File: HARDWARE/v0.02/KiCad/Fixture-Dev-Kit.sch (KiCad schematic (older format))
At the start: 6 parts, among them J1 DUT, J2 POWER, J39 DUT BAT, J40 DUT BAT

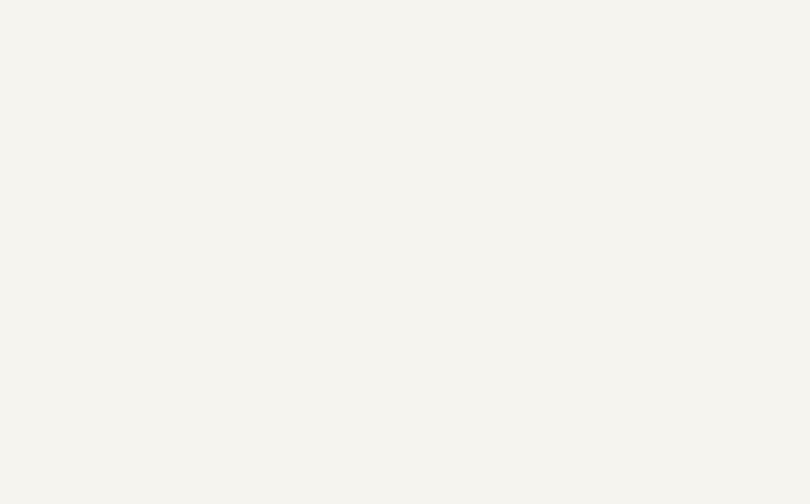
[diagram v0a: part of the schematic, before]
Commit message: adding latest updates from pcb layout designed 11/8/2017
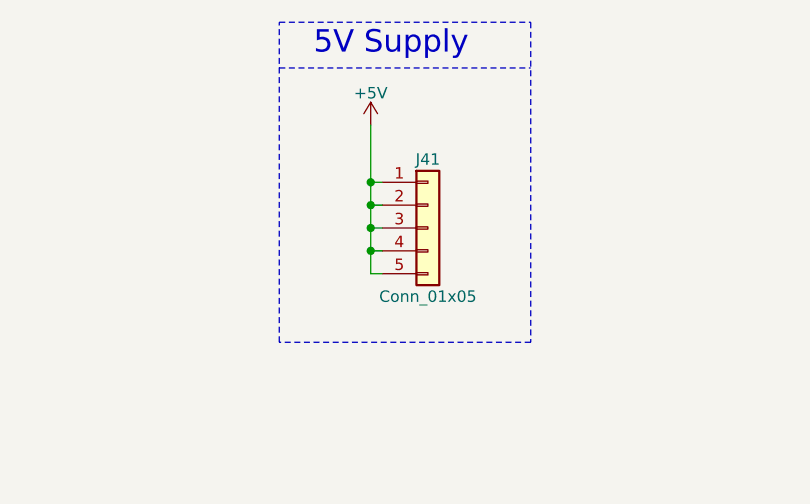
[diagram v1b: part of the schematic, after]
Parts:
- added J41: Conn_01x05, Pin_Headers:Pin_Header_Angled_1x05_Pitch2.54mm, symbol Conn_01x05
- J39: footprint Connectors_JST:JST_PH_B2B-PH-K_02x2.00mm_Straight -> Connectors_JST:JST_PH_S2B-PH-K_02x2.00mm_Angled
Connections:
- wire segments 50 -> 56
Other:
- note added: "5V Supply\n"
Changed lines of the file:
@@
 LIBS:TCA6424ARGJR
 LIBS:USB-A1HSW6
+LIBS:jumper
 LIBS:Fixture-Dev-Kit-cache
 EELAYER 25 0
@@
 $EndComp
 $Comp
-L GND #PWR9
+L GND #PWR2
 U 1 1 59EFDED6
 P 1700 5100
-F 0 "#PWR9" H 1700 4850 50  0001 C CNN
+F 0 "#PWR2" H 1700 4850 50  0001 C CNN
 F 1 "GND" H 1700 4950 50  0000 C CNN
 F 2 "" H 1700 5100 50  0001 C CNN
@@
 	1550 4350 1800 4350
 $Comp
-L GND #PWR7
+L GND #PWR4
 U 1 1 59F1B0B1
 P 1800 4450
-F 0 "#PWR7" H 1800 4200 50  0001 C CNN
+F 0 "#PWR4" H 1800 4200 50  0001 C CNN
 F 1 "GND" H 1800 4300 50  0000 C CNN
 F 2 "" H 1800 4450 50  0001 C CNN
@@
 	850  4000 2550 4000
 $Comp
-L +5V #PWR8
+L +5V #PWR1
 U 1 1 59F1DD6A
 P 1200 5100
-F 0 "#PWR8" H 1200 4950 50  0001 C CNN
+F 0 "#PWR1" H 1200 4950 50  0001 C CNN
 F 1 "+5V" H 1200 5240 50  0000 C CNN
 F 2 "" H 1200 5100 50  0001 C CNN
@@
 $EndComp
 $Comp
-L +5V #PWR6
+L +5V #PWR3
 U 1 1 59F1DD81
 P 1800 4350
-F 0 "#PWR6" H 1800 4200 50  0001 C CNN
+F 0 "#PWR3" H 1800 4200 50  0001 C CNN
 F 1 "+5V" H 1800 4490 50  0000 C CNN
 F 2 "" H 1800 4350 50  0001 C CNN
@@
 $EndSheet
 $Comp
-L GND #PWR5
+L GND #PWR10
 U 1 1 59FA7F5A
 P 9250 4050
-F 0 "#PWR5" H 9250 3800 50  0001 C CNN
+F 0 "#PWR10" H 9250 3800 50  0001 C CNN
 F 1 "GND" H 9250 3900 50  0000 C CNN
 F 2 "" H 9250 4050 50  0001 C CNN
@@
 	2650 1600 2500 1600
 $Comp
-L +5V #PWR1
+L +5V #PWR5
 U 1 1 59FB980B
 P 2650 1950
-F 0 "#PWR1" H 2650 1800 50  0001 C CNN
+F 0 "#PWR5" H 2650 1800 50  0001 C CNN
 F 1 "+5V" H 2650 2090 50  0000 C CNN
 F 2 "" H 2650 1950 50  0001 C CNN
@@
 	6850 3200 6700 3200
 $Comp
-L +5V #PWR3
+L +5V #PWR6
 U 1 1 59FC47B7
 P 4500 3050
-F 0 "#PWR3" H 4500 2900 50  0001 C CNN
+F 0 "#PWR6" H 4500 2900 50  0001 C CNN
 F 1 "+5V" H 4500 3190 50  0000 C CNN
 F 2 "" H 4500 3050 50  0001 C CNN
@@
 $EndComp
 $Comp
-L +5V #PWR4
+L +5V #PWR8
 U 1 1 59FC49D9
 P 6900 3100
-F 0 "#PWR4" H 6900 2950 50  0001 C CNN
+F 0 "#PWR8" H 6900 2950 50  0001 C CNN
 F 1 "+5V" H 6900 3240 50  0000 C CNN
 F 2 "" H 6900 3100 50  0001 C CNN
@@
 F 0 "J39" H 8400 4550 50  0000 C CNN
 F 1 "DUT BAT" H 8400 4250 50  0000 C CNN
-F 2 "Connectors_JST:JST_PH_B2B-PH-K_02x2.00mm_Straight" H 8400 4450 50  0001 C CNN
+F 2 "Connectors_JST:JST_PH_S2B-PH-K_02x2.00mm_Angled" H 8400 4450 50  0001 C CNN
 F 3 "" H 8400 4450 50  0001 C CNN
 	1    8400 4450
@@
 Connection ~ 8700 3850
 $Comp
-L +5V #PWR2
+L +5V #PWR9
 U 1 1 5A01083F
 P 8050 2750
-F 0 "#PWR2" H 8050 2600 50  0001 C CNN
+F 0 "#PWR9" H 8050 2600 50  0001 C CNN
 F 1 "+5V" H 8050 2890 50  0000 C CNN
 F 2 "" H 8050 2750 50  0001 C CNN
@@
 Wire Wire Line
 	7850 3050 7850 3250
+$Comp
+L Conn_01x05 J41
+U 1 1 5A02A9A2
+P 5350 1600
+F 0 "J41" H 5350 1900 50  0000 C CNN
+F 1 "Conn_01x05" H 5350 1300 50  0000 C CNN
+F 2 "Pin_Headers:Pin_Header_Angled_1x05_Pitch2.54mm" H 5350 1600 50  0001 C CNN
+F 3 "" H 5350 1600 50  0001 C CNN
+	1    5350 1600
+	1    0    0    -1
+$EndComp
+$Comp
+L +5V #PWR7
+U 1 1 5A02AD38
+P 5100 1150
+F 0 "#PWR7" H 5100 1000 50  0001 C CNN
+F 1 "+5V" H 5100 1290 50  0000 C CNN
+F 2 "" H 5100 1150 50  0001 C CNN
+F 3 "" H 5100 1150 50  0001 C CNN
+	1    5100 1150
+	1    0    0    -1
+$EndComp
+Wire Wire Line
+	5100 1150 5100 1800
+Wire Wire Line
+	5100 1800 5150 1800
+Wire Wire Line
+	5150 1700 5100 1700
+Connection ~ 5100 1700
+Wire Wire Line
+	5150 1600 5100 1600
+Connection ~ 5100 1600
+Wire Wire Line
+	5150 1500 5100 1500
+Connection ~ 5100 1500
+Wire Wire Line
+	5150 1400 5100 1400
+Connection ~ 5100 1400
+Wire Notes Line
+	4700 900  5800 900
+Wire Notes Line
+	5800 700  5800 2100
+Wire Notes Line
+	5800 2100 4700 2100
+Wire Notes Line
+	4700 2100 4700 700
+Wire Notes Line
+	4700 700  5800 700
+Text Notes 4850 850  0    98   ~ 0
+5V Supply\n
 $EndSCHEMATC
